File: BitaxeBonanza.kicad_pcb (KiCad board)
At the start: 6 copper layers, 76 x 87.5 mm, 272 parts, among them J1 XT30, J2 Conn_01x03, J4 Conn_01x04, J5 Conn_01x12, J6 USB_C_Receptacle_USB2.0, Q1 BSS138, SW3 SWITCH-SPST, SW4 SWITCH-SPST, U1 MCP1824T-1202E/OT, U11 RP2040, U12 ESP32-S3-WROOM-1, U13 TPS62933DRLR, U14 TPS62933DRLR, U15 STHW4-DU-HN050206, U16 STHW4-DU-HN050206, U17 STHW4-DU-HN050206, U2 TPS546D24SRVFR, U3 MCP1824T-1202E/OT, U4 MCP1824T-1202E/OT, U5 W25Q16JVUXIQ TR, U6 MCP1824T-1202E/OT, U8 SN74AXC4T774, U9 TPS22919DCKR, Y1 12MHz, Y2 50MHz

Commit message: adding jlcpcb deets
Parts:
- moved TP61 13.0 mm to (103.7, 55.8)
- moved TP10 1.36 mm to (109.8, 99.9)
- moved C2 1.26 mm to (110.4, 76.8)
- moved C14 0.14 mm to (125.8, 87.4)
- moved C13 0.13 mm to (124.7, 87.4)
- moved C9 0.13 mm to (123.4, 87.4)
- moved C5 0.13 mm to (118.8, 87.4)
- moved C6 0.13 mm to (121.3, 87.4)
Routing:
- net /5V_SWITCH: track 167.0 -> 169.8 mm
- net /12V: track 78.4 -> 80.5 mm, vias 45 -> 77
- net /Data/EN: track 87.9 -> 88.6 mm
- net /ASIC/1V2-1: track 64.5 -> 63.9 mm
- net /ASIC/REFCLKIN1: track 8.03 -> 7.49 mm
- net /ASIC/GND3: track 112.9 -> 113.5 mm
- net GND: track 47.9 -> 47.7 mm, vias 279 -> 325

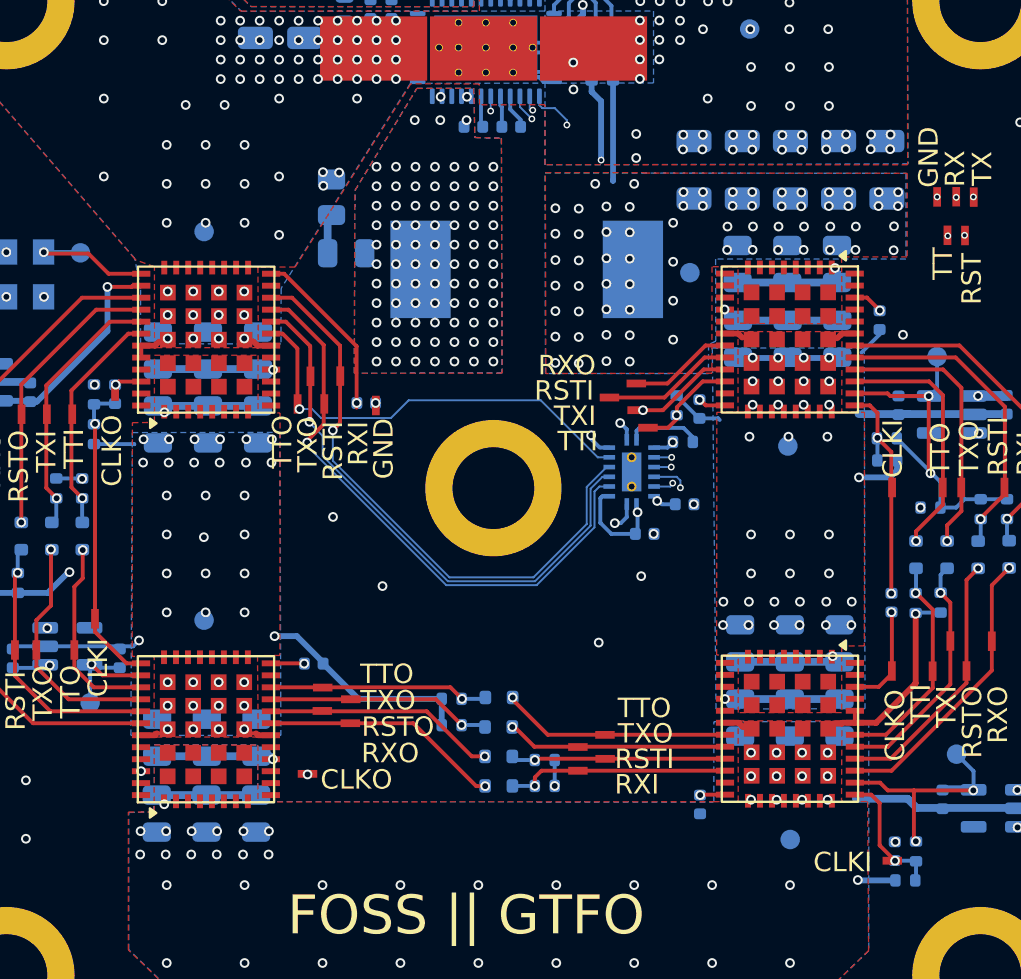
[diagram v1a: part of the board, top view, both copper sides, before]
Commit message: switched 100uF ASIC domain bypass caps to cheaper 1206
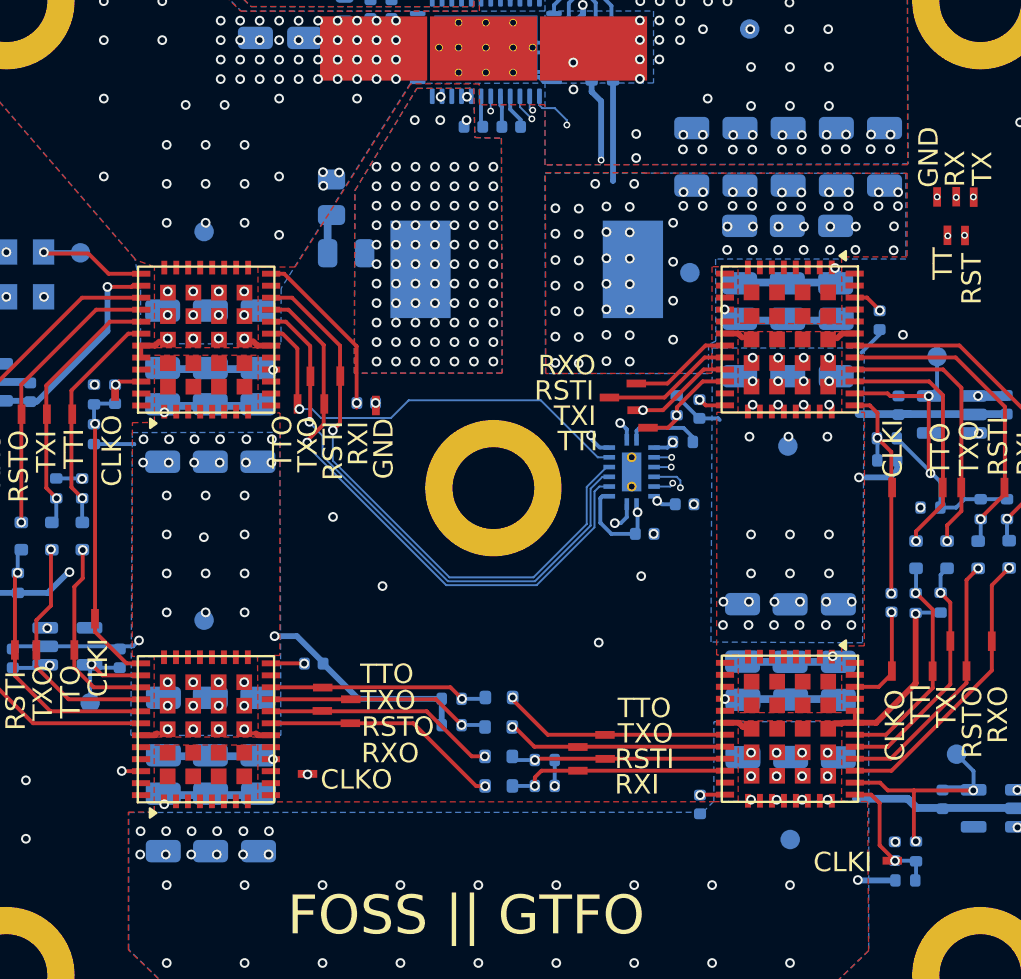
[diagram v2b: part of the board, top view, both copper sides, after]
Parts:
- C100, C101, C107, C108, C109, C115, C116, C117, C123, C124, C125, C131, C132, C133, C139, C140, C141, C83, C84, C85, C91, C92, C93, C99: footprint Capacitor_SMD:C_0805_2012Metric -> Capacitor_SMD:C_1206_3216Metric
- moved C21 0.68 mm to (148.6, 95.0)
- moved C22 0.68 mm to (146.1, 95.0)
- moved C24 0.68 mm to (141.2, 95.0)
- moved C20 0.68 mm to (151.1, 95.0)
- moved C23 0.68 mm to (143.7, 95.0)
- moved C107 0.66 mm to (114.1, 124.2)
- moved C91 0.63 mm to (114.0, 104.4)
- moved C108 0.60 mm to (116.5, 124.2)
- moved C92 0.59 mm to (116.5, 104.4)
- moved C125 0.58 mm to (143.8, 124.3)
- moved C93 0.58 mm to (118.9, 104.4)
- moved C109 0.58 mm to (118.9, 124.2)
- moved C123 0.57 mm to (148.7, 124.3)
- moved C99 0.56 mm to (114.0, 129.2)
- moved C124 0.55 mm to (146.3, 124.3)
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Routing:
- net /ASIC/GND4: track 73.2 -> 68.1 mm
- net /ASIC/REFCLKOUT2: track 40.9 -> 42.9 mm

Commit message: switch to in stock USB connector
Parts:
- J6: value USB_C_Receptacle_USB2.0 -> TYPE-C-31-M-12; footprint bitaxe:USB_C_Receptacle_GCT_USB4105-xx-A -> bitaxe:USB-C_SMD-TYPE-C-31-M-12_1
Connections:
- TP64 pad 1: Net-(J6-VBUS-PadA4) -> Net-(J6-VBUS-PadA4B9)
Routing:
- net Net-(J6-VBUS-PadA4B9): track 0.00 -> 12.8 mm
- net Net-(J6-VBUS-PadA4): track 12.8 -> 0.00 mm
